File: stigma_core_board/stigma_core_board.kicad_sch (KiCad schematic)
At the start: 93 parts, among them J1 TC2050, J5 USB_C_Receptacle_USB2.0, SW1 KMR721NGLFS, SW2 KMR721NGLFS, U1 STM32H743VITx, U10 H3LIS331DL, U11 MS5607/MS5611, U12 LIS3MDL, U13 BMP580, U2 TPD4E1U06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

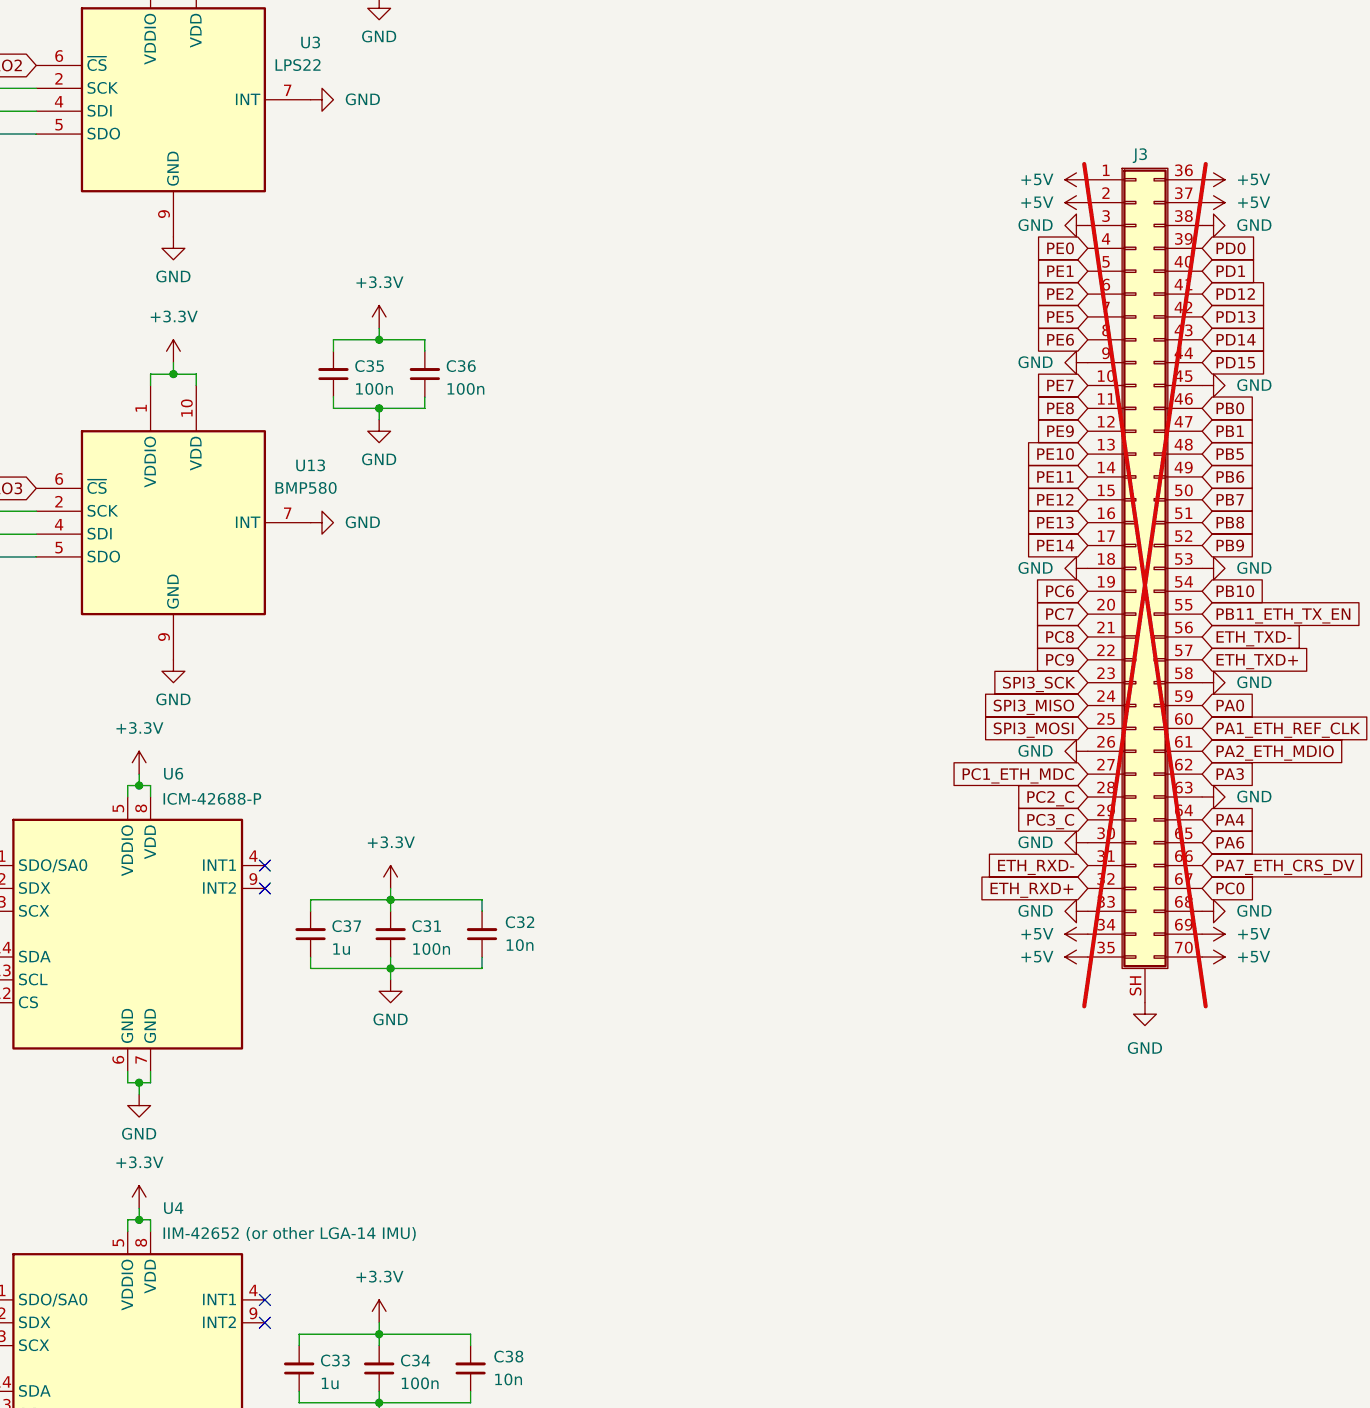
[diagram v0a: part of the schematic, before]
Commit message: Minor routing tweaks, add net colors
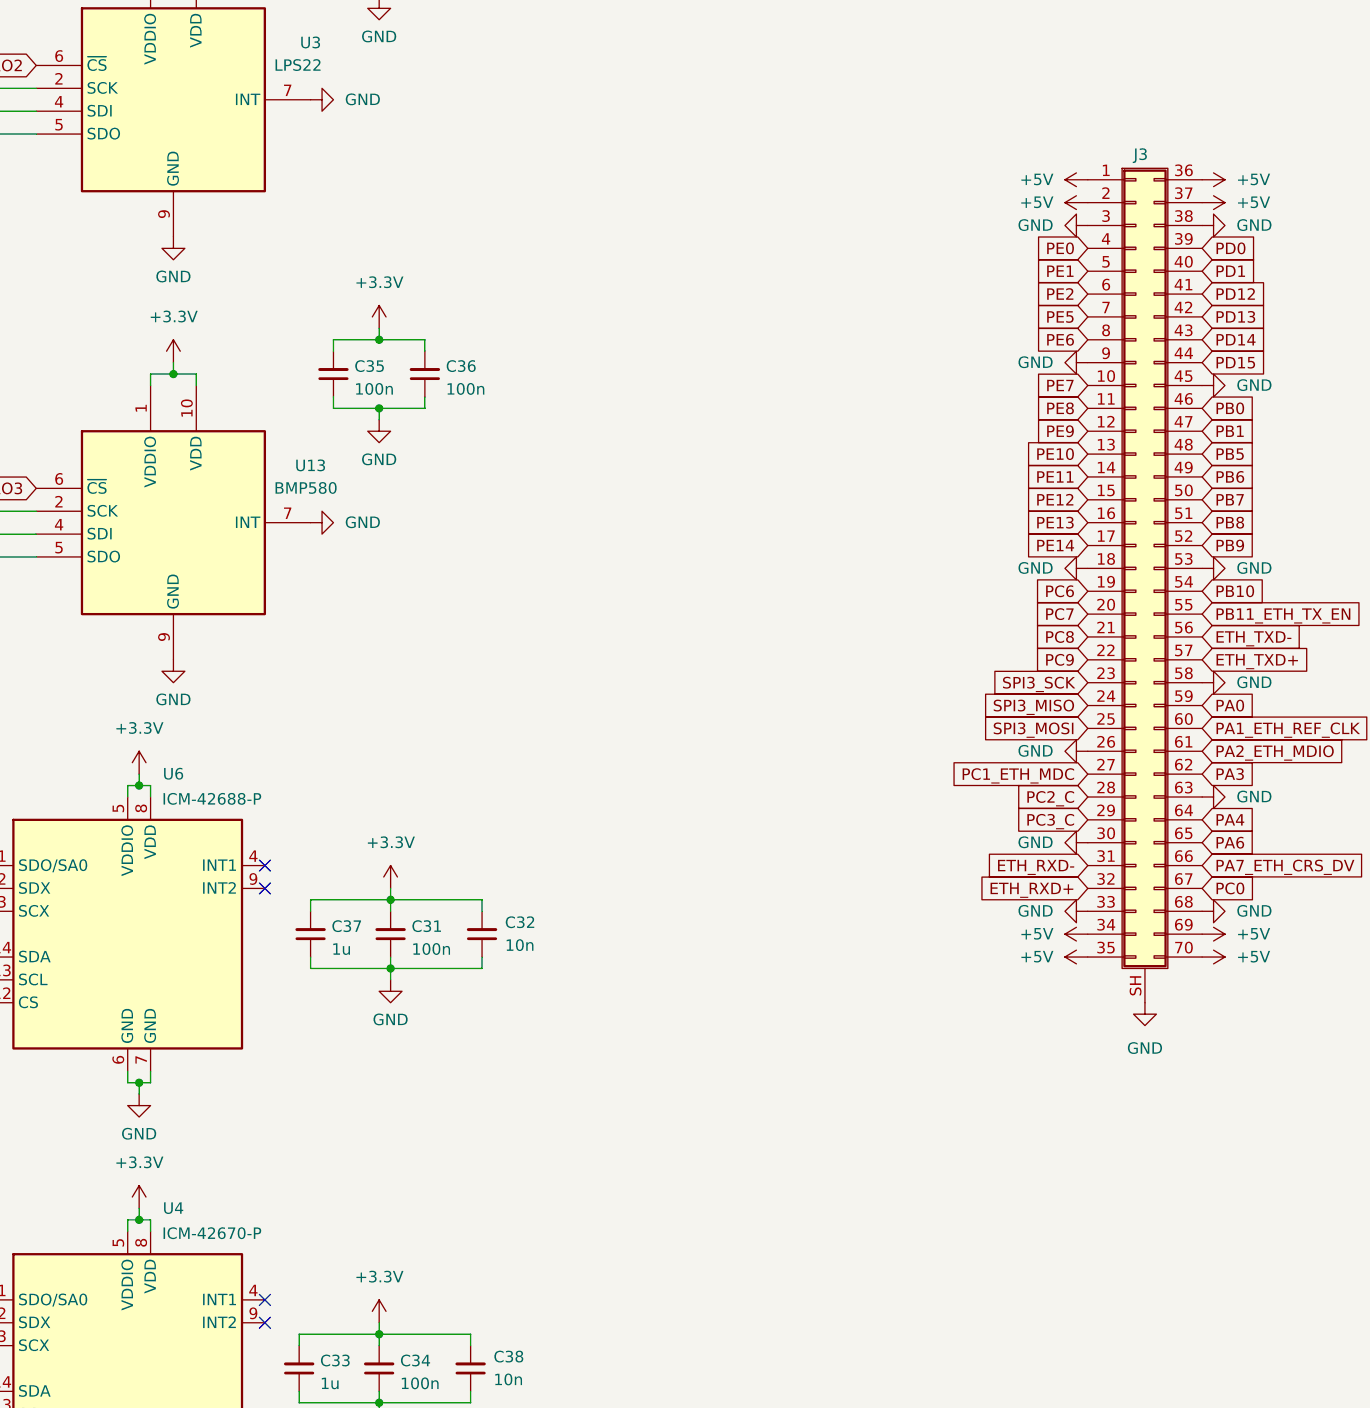
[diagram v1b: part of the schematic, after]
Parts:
- J3: now fitted; now left out of the parts list
- U4: value IIM-42652 (or other LGA-14 IMU) -> ICM-42670-P; LCSC C2988404 -> C3288646; Manufacturer STMicroelectronics -> (none); Part# LSM6DSRTR -> (none)
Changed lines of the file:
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@@
 			)
 		)
-		(property "Value" "IIM-42652 (or other LGA-14 IMU)"
+		(property "Value" "ICM-42670-P"
 			(at 248.92 175.514 0)
 			(effects
@@
 			)
 		)
-		(property "Datasheet" "https://www.st.com/resource/en/datasheet/lsm6ds3tr-c.pdf"
+		(property "Datasheet" ""
 			(at 247.65 207.01 0)
 			(effects
@@
 			)
 		)
-		(property "LCSC" "C2988404"
+		(property "LCSC" "C3288646"
 			(at 245.11 190.5 0)
 			(effects
@@
 			)
 		)
-		(property "Manufacturer" "STMicroelectronics"
+		(property "Manufacturer" ""
 			(at 245.11 190.5 0)
 			(effects
@@
 			)
 		)
-		(property "Part#" "LSM6DSRTR"
+		(property "Part#" ""
 			(at 245.11 190.5 0)
 			(effects
@@
 		(unit 1)
 		(exclude_from_sim no)
-		(in_bom yes)
+		(in_bom no)
 		(on_board yes)
-		(dnp yes)
+		(dnp no)
 		(property "Reference" "J3"
 			(at 356.87 55.626 0)

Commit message: minor changes
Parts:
- R12, R13: value 22 -> 22R
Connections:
- net VCAP1: now reaches C9.1, U1.48 (VCAP)
- net VCAP2: now reaches C10.1, U1.73 (VCAP)
- net J1-SWO: now reaches J1.5 (Pin_5), R19.2, U7.1 (IO1)
- net J1-SWDIO: now reaches J1.2 (Pin_2), R18.2, U7.2 (IO2)
- net VBUS: now reaches C40.2, D4.2 (A), J5.A4 (VBUS), J5.A9 (VBUS), J5.B4 (VBUS), J5.B9 (VBUS), R14.2, U2.6 (V_{cc})
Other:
- note added: "128 Mbit"
- note added: "flash"
- note added: "should have 90Ohms of impedance!"
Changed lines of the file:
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@@
 	(wire
 		(pts
+			(xy 95.25 236.22) (xy 95.25 237.49)
+		)
+		(stroke
+			(width 0)
+			(type default)
+		)
+	)
+	(wire
+		(pts
 			(xy 247.65 125.73) (xy 247.65 127)
 		)
@@
 	(wire
 		(pts
+			(xy 73.66 215.9) (xy 90.17 215.9)
+		)
+		(stroke
+			(width 0)
+			(type default)
+		)
+	)
+	(wire
+		(pts
 			(xy 38.1 215.9) (xy 41.91 215.9)
 		)
@@
 		)
 	)
+	(rectangle
+		(start 317.5 191.77)
+		(end 388.62 246.38)
+		(stroke
+			(width 0)
+			(type default)
+		)
+		(fill
+			(type none)
+		)
+	)
 	(text "TODO: double check pinout"
 		(exclude_from_sim no)
@@
 		)
 	)
+	(text "128 Mbit"
+		(exclude_from_sim no)
+		(at 328.676 201.168 0)
+		(effects
+			(font
+				(size 1.27 1.27)
+			)
+		)
+	)
 	(text "Of the two USB peripherals, we use\nthis one, because PA11/PA12 are what\nthe bootloader uses for DFU."
 		(exclude_from_sim no)
@@
 		)
 	)
+	(text "flash"
+		(exclude_from_sim no)
+		(at 319.786 190.754 0)
+		(effects
+			(font
+				(size 1.27 1.27)
+				(thickness 0.254)
+				(bold yes)
+			)
+		)
+	)
 	(text "When substituting with a different 1117,\nensure compatibility with low-ESR\nceramic output capacitors."
 		(exclude_from_sim no)
@@
 		)
 	)
+	(text "should have 90Ohms of impedance!"
+		(exclude_from_sim no)
+		(at 211.328 250.444 0)
+		(effects
+			(font
+				(size 1.27 1.27)
+			)
+		)
+	)
 	(text "TODO: load cap values"
 		(exclude_from_sim no)
@@
 		)
 	)
+	(label "VCAP1"
+		(at 16.51 163.83 0)
+		(fields_autoplaced yes)
+		(effects
+			(font
+				(size 1.27 1.27)
+			)
+			(justify left bottom)
+		)
+	)
 	(label "D0+"
 		(at 223.52 243.84 180)
@@
 		)
 	)
+	(label "J1-SWCLK"
+		(at 101.6 228.6 0)
+		(fields_autoplaced yes)
+		(effects
+			(font
+				(size 1.27 1.27)
+			)
+			(justify left bottom)
+		)
+	)
+	(label "J1-SWO"
+		(at 77.47 234.95 0)
+		(fields_autoplaced yes)
+		(effects
+			(font
+				(size 1.27 1.27)
+			)
+			(justify left bottom)
+		)
+	)
+	(label "VBUS"
+		(at 218.44 217.17 0)
+		(fields_autoplaced yes)
+		(effects
+			(font
+				(size 1.27 1.27)
+			)
+			(justify left bottom)
+		)
+	)
 	(label "D0-"
 		(at 223.52 238.76 180)
@@
 		)
 	)
+	(label "J1-SWDIO"
+		(at 81.28 218.44 0)
+		(fields_autoplaced yes)
+		(effects
+			(font
+				(size 1.27 1.27)
+			)
+			(justify left bottom)
+		)
+	)
+	(label "VCAP2"
+		(at 25.4 166.37 0)
+		(fields_autoplaced yes)
+		(effects
+			(font
+				(size 1.27 1.27)
+			)
+			(justify left bottom)
+		)
+	)
 	(global_label "SPI3_SCK"
 		(shape input)
@@
 	(global_label "NRST"
 		(shape input)
-		(at 90.17 215.9 180)
+		(at 73.66 215.9 180)
 		(fields_autoplaced yes)
 		(effects
@@
 		)
 		(property "Intersheetrefs" "${INTERSHEET_REFS}"
-			(at 82.4072 215.9 0)
+			(at 65.8972 215.9 0)
 			(effects
 				(font
@@
 		(dnp no)
 		(property "Reference" "R13"
-			(at 215.265 247.015 90)
+			(at 214.884 246.888 90)
 			(effects
 				(font
@@
 			)
 		)
-		(property "Value" "22"
-			(at 215.265 248.92 90)
+		(property "Value" "22R"
+			(at 218.948 246.888 90)
 			(effects
 				(font
@@
 	(symbol
 		(lib_id "power:+5V")
-		(at 95.25 237.49 0)
+		(at 95.25 236.22 0)
 		(unit 1)
 		(exclude_from_sim no)
@@
 		(fields_autoplaced yes)
 		(property "Reference" "#PWR0102"
-			(at 95.25 241.3 0)
+			(at 95.25 240.03 0)
 			(effects
 				(font
@@
 		)
 		(property "Value" "+5V"
-			(at 95.25 232.41 0)
+			(at 95.25 231.14 0)
 			(effects
 				(font
@@
 		)
 		(property "Footprint" ""
-			(at 95.25 237.49 0)
+			(at 95.25 236.22 0)
 			(effects
 				(font
@@
 		)
 		(property "Datasheet" ""
-			(at 95.25 237.49 0)
+			(at 95.25 236.22 0)
 			(effects
 				(font
@@
 		)
 		(property "Description" "Power symbol creates a global label with name \"+5V\""
-			(at 95.25 237.49 0)
+			(at 95.25 236.22 0)
 			(effects
 				(font
@@
 			)
 		)
-		(property "Datasheet" "https://www.diodes.com/assets/Datasheets/AZ1117.pdf"
+		(property "Datasheet" "https://www.diodes.com/assets/Datasheets/AZ1117I.pdf"
 			(at 146.05 252.73 0)
 			(effects
@@
 		(dnp no)
 		(property "Reference" "R12"
-			(at 215.265 236.22 90)
+			(at 217.17 238.252 90)
 			(effects
 				(font
@@
 			)
 		)
-		(property "Value" "22"
-			(at 215.265 238.125 90)
+		(property "Value" "22R"
+			(at 217.424 242.062 90)
 			(effects
 				(font
@@
 		(on_board yes)
 		(dnp no)
-		(fields_autoplaced yes)
 		(property "Reference" "U2"
-			(at 203.6765 251.46 0)
+			(at 202.946 253.238 0)
 			(effects
 				(font
@@
 		)
 		(property "Value" "TPD4E1U06"
-			(at 203.6765 254 0)
+			(at 202.946 255.27 0)
 			(effects
 				(font

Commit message: Add correct load capacitors, tweak USB routing, fab options
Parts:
- C11, C12: value 3.9p -> 10p; LCSC (none) -> C32949
- C13, C14: value 1.5p -> 10p; LCSC (none) -> C32949
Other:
- note removed: "TODO: double check pinout"
- note removed: "TODO: load cap values"
- note removed: "should have 90Ohms of impedance!"
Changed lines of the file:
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@@
 		)
 	)
-	(text "TODO: double check pinout"
-		(exclude_from_sim no)
-		(at 107.95 194.31 0)
-		(effects
-			(font
-				(size 1.27 1.27)
-			)
-		)
-	)
 	(text "128 Mbit"
 		(exclude_from_sim no)
@@
 		)
 	)
-	(text "should have 90Ohms of impedance!"
-		(exclude_from_sim no)
-		(at 211.328 250.444 0)
-		(effects
-			(font
-				(size 1.27 1.27)
-			)
-		)
-	)
-	(text "TODO: load cap values"
-		(exclude_from_sim no)
-		(at 40.64 198.12 0)
-		(effects
-			(font
-				(size 1.27 1.27)
-			)
-		)
-	)
 	(label "VCAP1"
 		(at 16.51 163.83 0)
@@
 			)
 		)
-		(property "Value" "1.5p"
+		(property "Value" "10p"
 			(at 30.988 235.966 0)
 			(effects
@@
 			)
 		)
-		(property "Description" "TODO"
+		(property "Description" "With Cs = 7pF and Cl = 12.5pF (Y1): Cext = 2 * (Cl - Cs) ~= 10pF"
+			(at 38.1 234.95 0)
+			(effects
+				(font
+					(size 1.27 1.27)
+				)
+				(hide yes)
+			)
+		)
+		(property "LCSC" "C32949"
 			(at 38.1 234.95 0)
 			(effects
@@
 			)
 		)
-		(property "Value" "3.9p"
+		(property "Value" "10p"
 			(at 48.26 214.6235 0)
 			(effects
@@
 			)
 		)
-		(property "Description" "TODO"
+		(property "Description" "With Cs = 7pF and Cl = 12pF (Y1): Cext = 2 * (Cl - Cs) = 10 pF"
+			(at 45.72 213.36 0)
+			(effects
+				(font
+					(size 1.27 1.27)
+				)
+				(hide yes)
+			)
+		)
+		(property "LCSC" "C32949"
 			(at 45.72 213.36 0)
 			(effects
@@
 			)
 		)
-		(property "Value" "1.5p"
+		(property "Value" "10p"
 			(at 48.26 236.2135 0)
 			(effects
@@
 			)
 		)
-		(property "Description" "TODO"
+		(property "Description" "With Cs = 7pF and Cl = 12.5pF (Y1): Cext = 2 * (Cl - Cs) ~= 10pF"
+			(at 45.72 234.95 0)
+			(effects
+				(font
+					(size 1.27 1.27)
+				)
+				(hide yes)
+			)
+		)
+		(property "LCSC" "C32949"
 			(at 45.72 234.95 0)
 			(effects
@@
 			)
 		)
-		(property "Value" "3.9p"
+		(property "Value" "10p"
 			(at 30.988 214.376 0)
 			(effects
@@
 			)
 		)
-		(property "Description" "TODO"
+		(property "Description" "With Cs = 7pF and Cl = 12pF (Y1): Cext = 2 * (Cl - Cs) = 10 pF"
+			(at 38.1 213.36 0)
+			(effects
+				(font
+					(size 1.27 1.27)
+				)
+				(hide yes)
+			)
+		)
+		(property "LCSC" "C32949"
 			(at 38.1 213.36 0)
 			(effects

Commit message: added 3d models of connectors
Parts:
- J3: value ~ -> CONN PLUG 70POS SMD GOLD; LCSC# (none) -> C2692097
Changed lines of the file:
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@@
 (kicad_sch
-	(version 20231120)
+	(version 20250114)
 	(generator "eeschema")
-	(generator_version "8.0")
+	(generator_version "9.0")
 	(paper "A3")
+	(rectangle
+		(start 317.5 191.77)
+		(end 388.62 246.38)
+		(stroke
+			(width 0)
+			(type default)
+		)
+		(fill
+			(type none)
+		)
+	)
+	(text "128 Mbit"
+		(exclude_from_sim no)
+		(at 328.676 201.168 0)
+		(effects
+			(font
+				(size 1.27 1.27)
+			)
+		)
+	)
+	(text "Of the two USB peripherals, we use\nthis one, because PA11/PA12 are what\nthe bootloader uses for DFU."
+		(exclude_from_sim no)
+		(at 85.852 85.344 0)
+		(effects
+			(font
+				(size 1.27 1.27)
+			)
+			(justify left)
+		)
+	)
+	(text "flash"
+		(exclude_from_sim no)
+		(at 319.786 190.754 0)
+		(effects
+			(font
+				(size 1.27 1.27)
+				(thickness 0.254)
+				(bold yes)
+			)
+		)
+	)
+	(text "When substituting with a different 1117,\nensure compatibility with low-ESR\nceramic output capacitors."
+		(exclude_from_sim no)
+		(at 128.27 276.86 0)
+		(effects
+			(font
+				(size 1.27 1.27)
+			)
+			(justify left bottom)
+		)
+	)
 	(junction
 		(at 41.91 30.48)
@@
 		)
 	)
-	(rectangle
-		(start 317.5 191.77)
-		(end 388.62 246.38)
-		(stroke
-			(width 0)
-			(type default)
-		)
-		(fill
-			(type none)
-		)
-	)
-	(text "128 Mbit"
-		(exclude_from_sim no)
-		(at 328.676 201.168 0)
-		(effects
-			(font
-				(size 1.27 1.27)
-			)
-		)
-	)
-	(text "Of the two USB peripherals, we use\nthis one, because PA11/PA12 are what\nthe bootloader uses for DFU."
-		(exclude_from_sim no)
-		(at 85.852 85.344 0)
-		(effects
-			(font
-				(size 1.27 1.27)
-			)
-			(justify left)
-		)
-	)
-	(text "flash"
-		(exclude_from_sim no)
-		(at 319.786 190.754 0)
-		(effects
-			(font
-				(size 1.27 1.27)
-				(thickness 0.254)
-				(bold yes)
-			)
-		)
-	)
-	(text "When substituting with a different 1117,\nensure compatibility with low-ESR\nceramic output capacitors."
-		(exclude_from_sim no)
-		(at 128.27 276.86 0)
-		(effects
-			(font
-				(size 1.27 1.27)
-			)
-			(justify left bottom)
-		)
-	)
 	(label "VCAP1"
 		(at 16.51 163.83 0)
-		(fields_autoplaced yes)
 		(effects
 			(font
@@
 	(label "D0+"
 		(at 223.52 243.84 180)
-		(fields_autoplaced yes)
 		(effects
 			(font
@@
 	(label "J1-SWCLK"
 		(at 101.6 228.6 0)
-		(fields_autoplaced yes)
 		(effects
 			(font
@@
 	(label "J1-SWO"
 		(at 77.47 234.95 0)
-		(fields_autoplaced yes)
 		(effects
 			(font
@@
 	(label "VBUS"
 		(at 218.44 217.17 0)
-		(fields_autoplaced yes)
 		(effects
 			(font
@@
 	(label "D0-"
 		(at 223.52 238.76 180)
-		(fields_autoplaced yes)
 		(effects
 			(font
@@
 	(label "J1-SWDIO"
 		(at 81.28 218.44 0)
-		(fields_autoplaced yes)
 		(effects
 			(font
@@
 	(label "VCAP2"
 		(at 25.4 166.37 0)
-		(fields_autoplaced yes)
 		(effects
 			(font
@@
 			)
 		)
-		(property "Value" "~"
+		(property "Value" "CONN PLUG 70POS SMD GOLD"
 			(at 356.8701 77.47 90)
 			(effects
@@
 			)
 		)
-		(property "Datasheet" "~"
+		(property "Datasheet" "https://www.hirose.com/en/product/document?clcode=&productname=&series=DF40&documenttype=Catalog&lang=en&documentid=en_DF40_CAT"
 			(at 356.87 101.6 0)
 			(effects
@@
 			)
 		)
+		(property "LCSC#" "C2692097"
+			(at 356.87 101.6 0)
+			(effects
+				(font
+					(size 1.27 1.27)
+				)
+				(hide yes)
+			)
+		)
 		(pin "36"
 		)
@@
 		)
 	)
+	(embedded_fonts no)
 )

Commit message: remove rst and boot from USB TSV diode
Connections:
- net BOOT: no longer U2.1 (IO1)
- net NRST: no longer U2.2 (IO2)
- no-connect marks 18 -> 20
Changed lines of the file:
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@@
 	)
 	(no_connect
+		(at 187.96 264.16)
+	)
+	(no_connect
 		(at 224.79 254)
 	)
@@
 	)
 	(no_connect
+		(at 187.96 269.24)
+	)
+	(no_connect
 		(at 173.99 95.25)
 	)
@@
 		)
 	)
-	(global_label "NRST"
-		(shape input)
-		(at 187.96 269.24 180)
-		(fields_autoplaced yes)
-		(effects
-			(font
-				(size 1.27 1.27)
-			)
-			(justify right)
-		)
-		(property "Intersheetrefs" "${INTERSHEET_REFS}"
-			(at 180.1972 269.24 0)
-			(effects
-				(font
-					(size 1.27 1.27)
-				)
-				(justify right)
-				(hide yes)
-			)
-		)
-	)
 	(global_label "LED_YELLOW"
 		(shape input)
@@
 				(hide yes)
 			)
-		)
-	)
-	(global_label "BOOT"
-		(shape input)
-		(at 187.96 264.16 180)
-		(fields_autoplaced yes)
-		(effects
-			(font
-				(size 1.27 1.27)
-			)
-			(justify right)
-		)
-		(property "Intersheetrefs" "${INTERSHEET_REFS}"
-			(at 180.0762 264.16 0)
-			(effects
-				(font
-					(size 1.27 1.27)
-				)
-				(justify right)
-				(hide yes)
-			)

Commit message: core: Replace flash w/ W25Q256, WSON 8x6
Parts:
- U8: value W25Q128JVP -> W25Q256JVEIQ; footprint Package_SON:WSON-8-1EP_6x5mm_P1.27mm_EP3.4x4.3mm -> Package_SON:WSON-8-1EP_8x6mm_P1.27mm_EP3.4x4.3mm; LCSC C190862 -> C97522
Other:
- note removed: "128 Mbit"
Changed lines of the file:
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@@
 		)
 	)
-	(text "128 Mbit"
-		(exclude_from_sim no)
-		(at 328.676 201.168 0)
-		(effects
-			(font
-				(size 1.27 1.27)
-			)
-		)
-	)
 	(text "Of the two USB peripherals, we use\nthis one, because PA11/PA12 are what\nthe bootloader uses for DFU."
 		(exclude_from_sim no)
@@
 			)
 		)
-		(property "Value" "W25Q128JVP"
+		(property "Value" "W25Q256JVEIQ"
 			(at 360.172 229.108 0)
 			(effects
@@
 			)
 		)
-		(property "Footprint" "Package_SON:WSON-8-1EP_6x5mm_P1.27mm_EP3.4x4.3mm"
+		(property "Footprint" "Package_SON:WSON-8-1EP_8x6mm_P1.27mm_EP3.4x4.3mm"
 			(at 351.79 196.85 0)
 			(effects
@@
 			)
 		)
-		(property "LCSC" "C190862"
+		(property "LCSC" "C97522"
 			(at 351.79 219.71 0)
 			(effects

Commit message: core: Connect VREF to VDDA
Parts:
- U1: value STM32H743VITx -> STM32H743VIT6; LCSC C730183 -> C114409
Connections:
- net +3.3V: no longer C2.1, C4.1, U1.20 (VREF+)
- net +3.3VA: now also C2.1, C4.1, U1.20 (VREF+)
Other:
- moved on the sheet: C16, C17, C2, C3, C4, C5, C6, C7, C8, FB1
